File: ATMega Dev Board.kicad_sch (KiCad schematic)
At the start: 48 parts, among them J1 Conn_01x13, J2 Conn_01x09, J4 SPI header, J5 USB-C_31-M-12, Q1 S8050, Q2 2N7002, Q3 HL6042, Q4 HL6042, SW1 SW_SPST, SW2 SW_SPST, U1 ATmega32A-A, U2 CH340C, U3 USBLC6-2P6, X1 16MHz

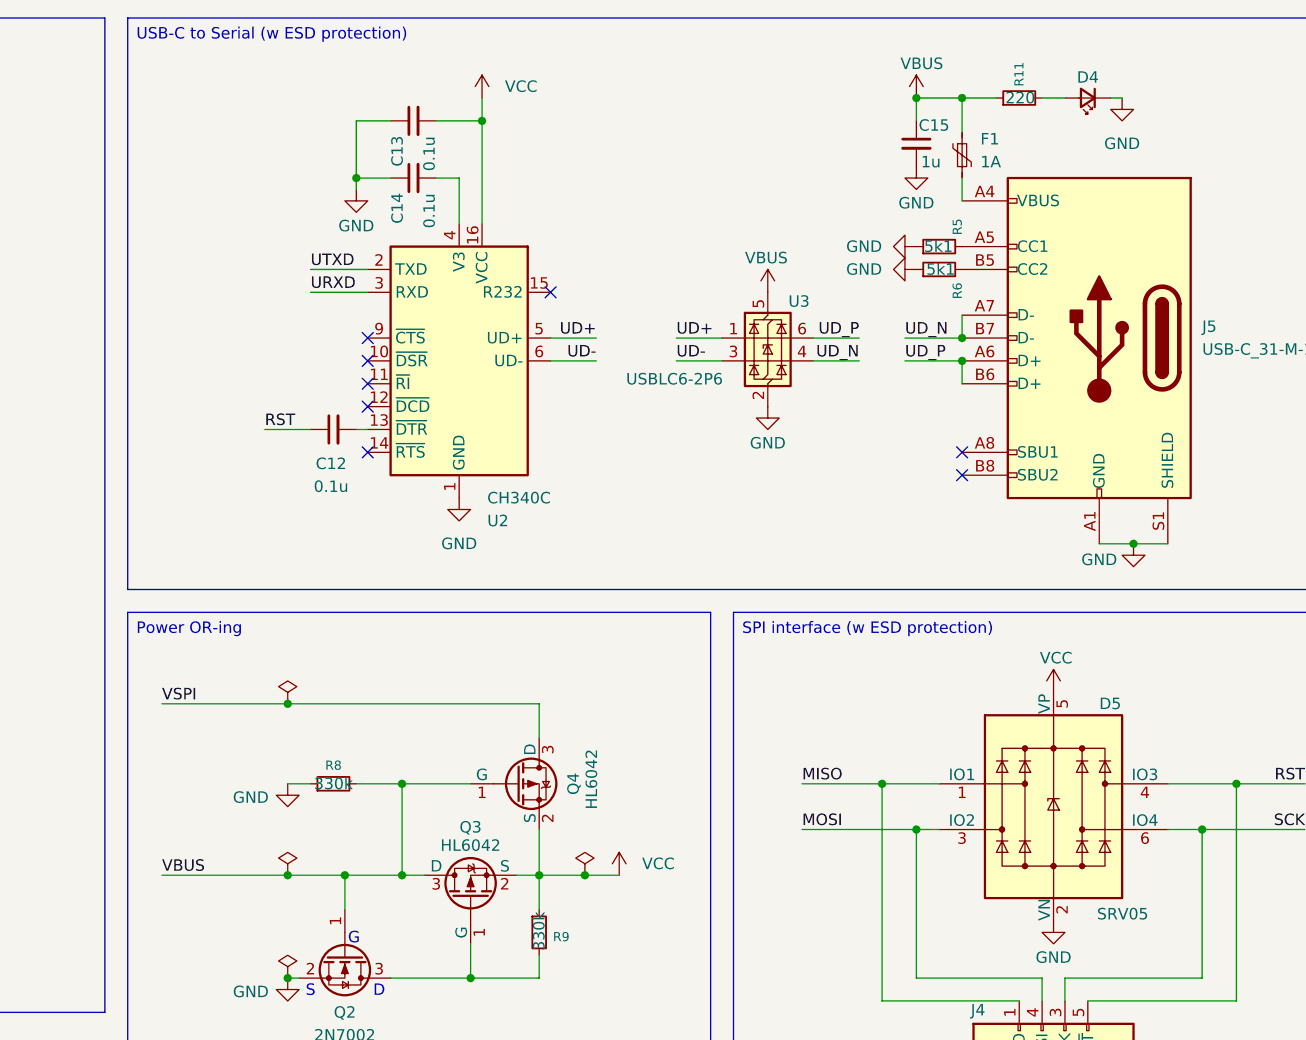
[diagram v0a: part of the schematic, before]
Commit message: better vbus power layout
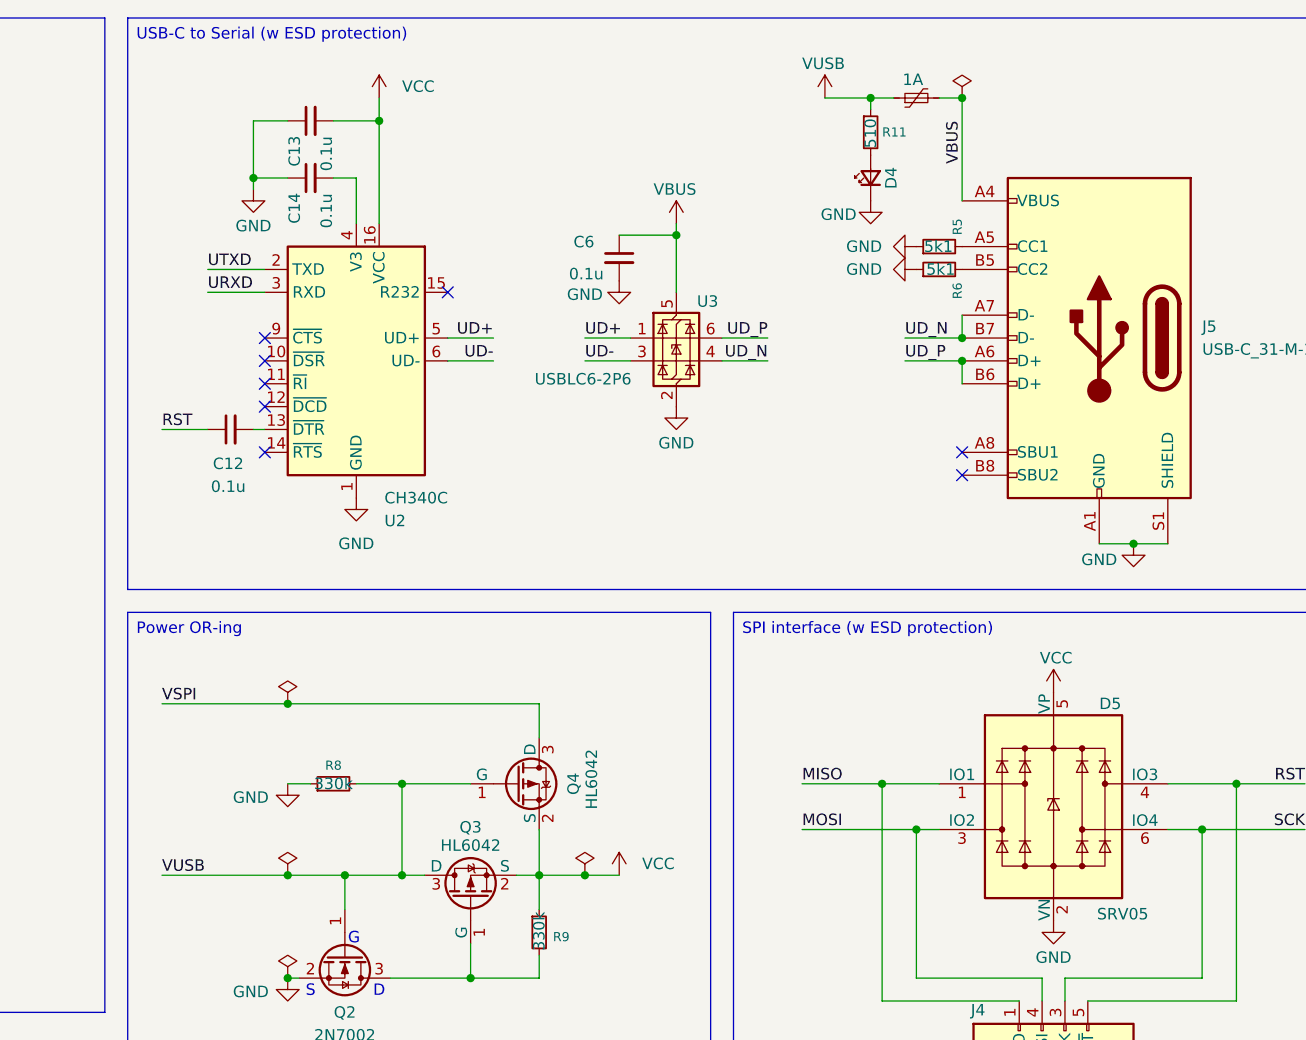
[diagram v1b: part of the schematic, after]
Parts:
- removed C15: 1u, Capacitor_SMD:C_0603_1608Metric, symbol Device:C_Small
- added C6: 0.1u, Capacitor_SMD:C_0603_1608Metric, symbol Device:C_Small
- J1, J2: now left out of the parts list
- Q3, Q4: footprint PCM_JLCPCB:Q_SOT-23 -> Package_TO_SOT_SMD:SOT-23
- R11: value 220 -> 510; LCSC C22962 -> C23193
- R5: footprint Resistor_SMD:R_0402_1005Metric -> Resistor_SMD:R_0603_1608Metric; LCSC C25905 -> C23186
- R6: footprint Resistor_SMD:R_0402_1005Metric -> Capacitor_SMD:C_0603_1608Metric; LCSC C25905 -> C23186
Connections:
- net GND: now also C6.2
- net VBUS: now also F1.2, J5.A4 (VBUS), J5.A9 (VBUS), J5.B4 (VBUS), J5.B9 (VBUS), C6.1; no longer F1.1, Q2.1 (G), Q3.3 (D), Q4.1 (G), R11.1, R8.2
- new net VUSB: F1.1, Q2.1 (G), Q3.3 (D), Q4.1 (G), R11.1, R8.2
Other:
- moved on the sheet: C12, C13, C14, D4, R11, U2, U3

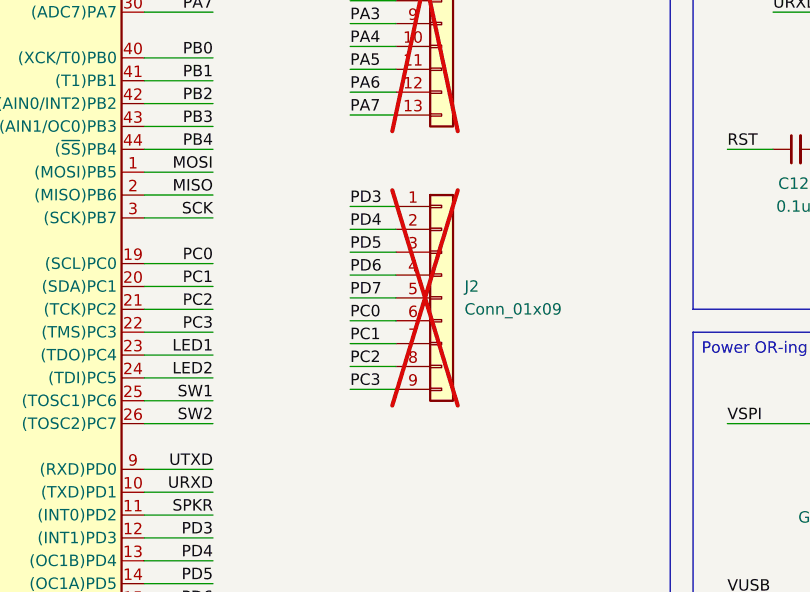
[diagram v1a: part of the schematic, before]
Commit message: exposed VCC and GND
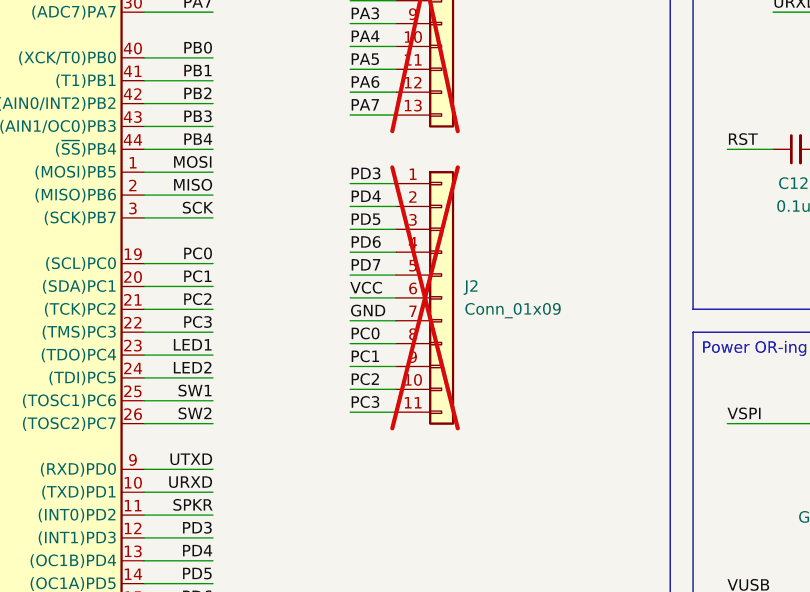
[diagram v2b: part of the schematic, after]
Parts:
- J2: footprint Connector_PinSocket_2.54mm:PinSocket_1x09_P2.54mm_Vertical -> Connector_PinSocket_2.54mm:PinSocket_1x11_P2.54mm_Vertical; symbol Connector_Generic:Conn_01x09 -> Connector_Generic:Conn_01x11; now in the parts list
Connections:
- net GND: now also J2.7 (Pin_7)
- net PC0: now also J2.8 (Pin_8); no longer J2.6 (Pin_6)
- net PC1: now also J2.9 (Pin_9); no longer J2.7 (Pin_7)
- net PC2: now also J2.10 (Pin_10); no longer J2.8 (Pin_8)
- net PC3: now also J2.11 (Pin_11); no longer J2.9 (Pin_9)
- net VCC: now also J2.6 (Pin_6)

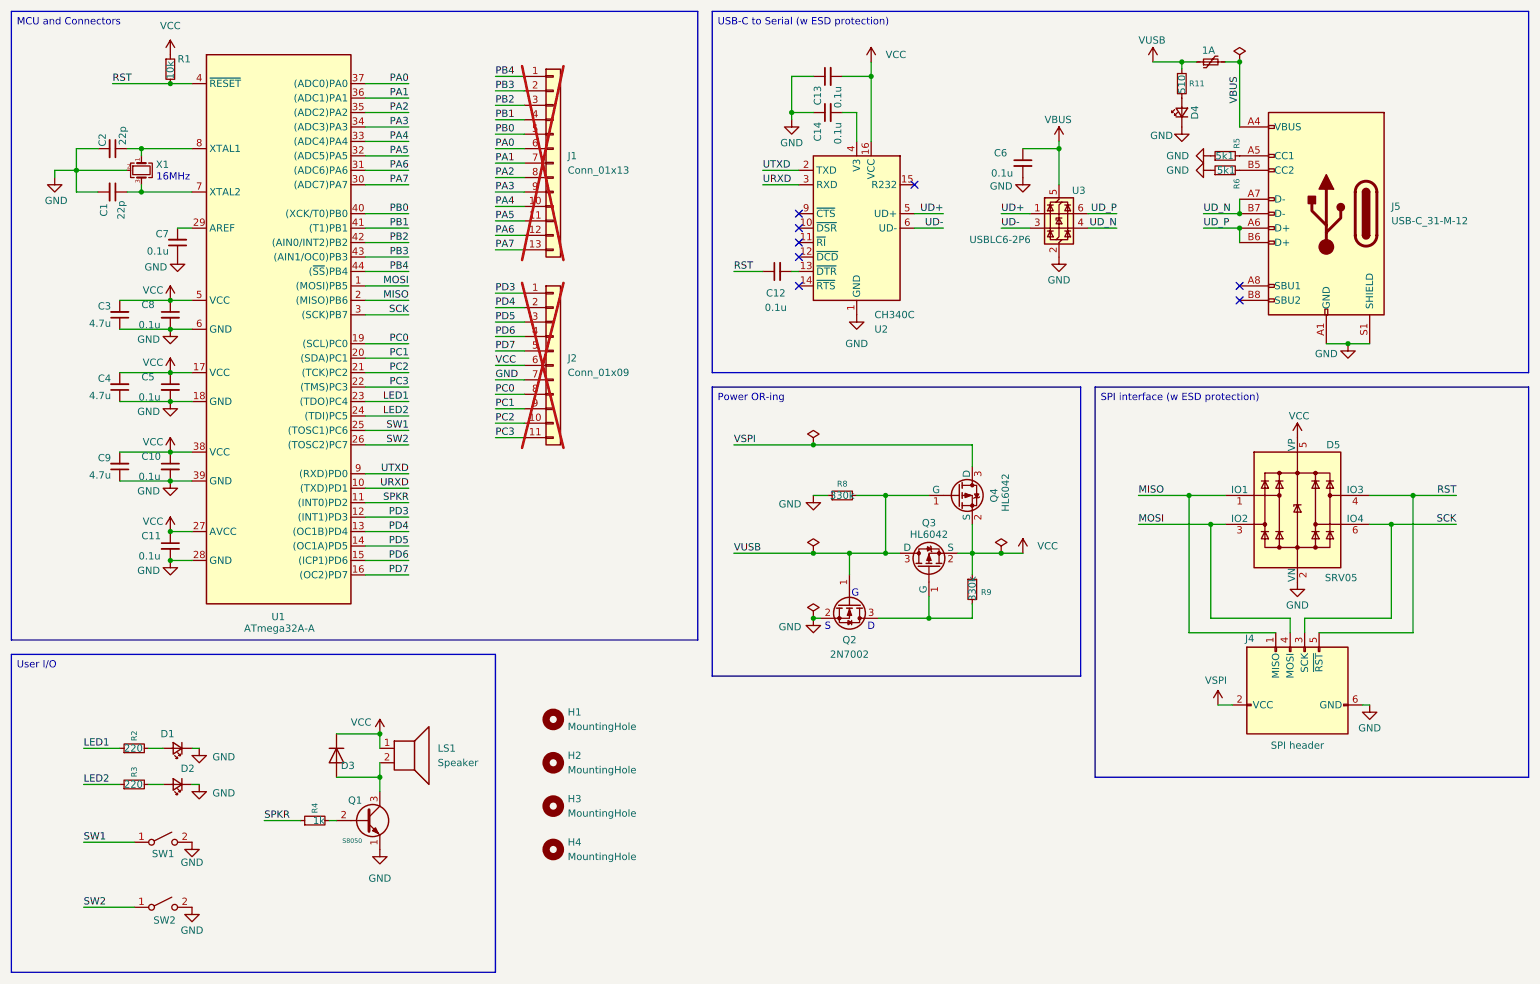
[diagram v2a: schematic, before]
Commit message: scl/sda pullups; better vcc filter
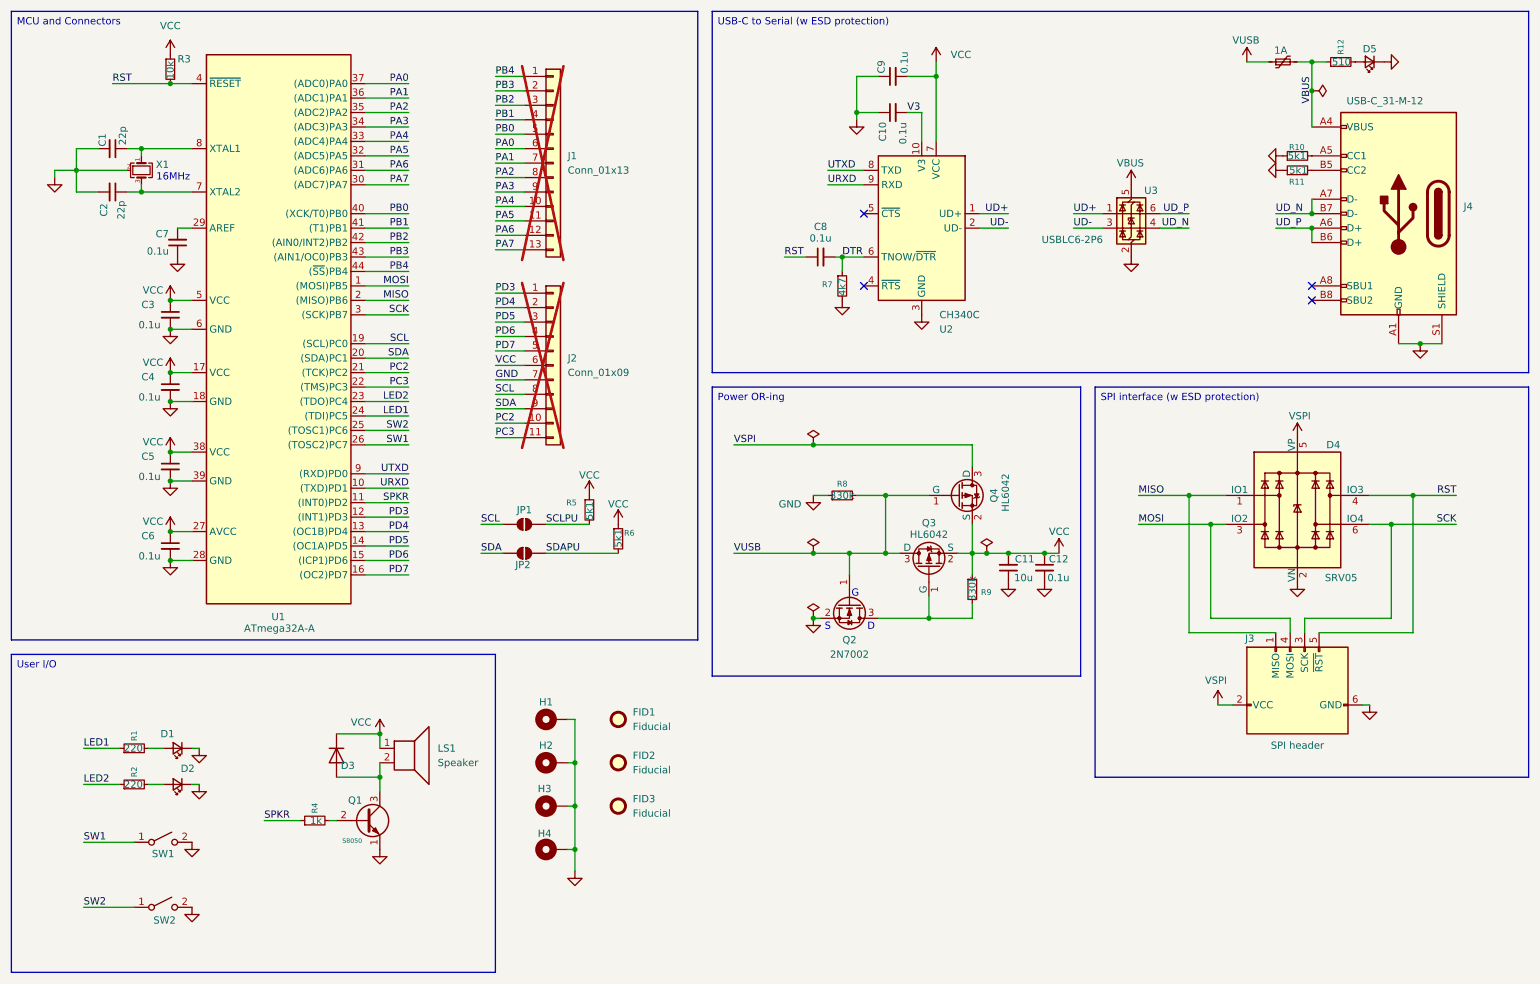
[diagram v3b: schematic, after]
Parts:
- removed C3, C4, C9: 4.7u, Capacitor_SMD:C_0603_1608Metric, symbol Device:C_Small
- removed C6: 0.1u, Capacitor_SMD:C_0603_1608Metric, symbol Device:C_Small
- added C11: 10u, Capacitor_SMD:C_0805_2012Metric, symbol Device:C_Small
- added C12: 0.1u, Capacitor_SMD:C_0603_1608Metric, symbol Device:C_Small
- added FID1, FID2, FID3: Fiducial, Fiducial:Fiducial_1mm_Mask2mm, symbol Mechanical:Fiducial
- added JP1, JP2: Jumper_2_Small_Open, Jumper:SolderJumper-2_P1.3mm_Open_Pad1.0x1.5mm, symbol Jumper:SolderJumper_2_Open
- added R5: 5k1, Capacitor_SMD:C_0603_1608Metric, symbol Device:R_Small
- added R6: 5k1, Resistor_SMD:R_0603_1608Metric, symbol Device:R_Small
- added R7: 4k7, Resistor_SMD:R_0603_1608Metric, symbol Device:R_Small
- H1, H2, H3, H4: footprint MountingHole:MountingHole_2.1mm -> MountingHole:MountingHole_3.2mm_M3_Pad_Via; symbol Mechanical:MountingHole -> Mechanical:MountingHole_Pad
- J4: renamed from J5; footprint FTBLib:USB_C_Receptacle_HRO_TYPE-C-31-M-12 -> ATMDBL:USB_C_Receptacle_HRO_TYPE-C-31-M-12
- LS1: footprint FTBLib:Buzzer_MLT-9650 -> ATMDBL:Buzzer_MLT-9650
- SW1, SW2: footprint FTBLib:Switch_TS-1088-AR02016 -> ATMDBL:Switch_TS-1088-AR02016
- U2: footprint Package_SO:SOIC-16_3.9x9.9mm_P1.27mm -> Package_SO:MSOP-10_3x3mm_P0.5mm; symbol Interface_USB:CH340C -> Interface_USB:CH340X
- renumbered C2 to C1, C14 to C10, C1 to C2, C8 to C3, C5 to C4, C10 to C5, C11 to C6, C12 to C8, C13 to C9, D5 to D4, D4 to D5, J4 to J3, R2 to R1, R5 to R10, R6 to R11, R11 to R12, R3 to R2, R1 to R3
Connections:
- net GND: now also H1.1, H2.1, H3.1, H4.1, U2.3 (GND), C11.1, C12.2, R7.2; no longer U2.1 (GND)
- net LED1: now also U1.24 ((TDI)PC5); no longer U1.23 ((TDO)PC4)
- net LED2: now also U1.23 ((TDO)PC4); no longer U1.24 ((TDI)PC5)
- net SW1: now also U1.26 ((TOSC2)PC7); no longer U1.25 ((TOSC1)PC6)
- net SW2: now also U1.25 ((TOSC1)PC6); no longer U1.26 ((TOSC2)PC7)
- net UD+: now also U2.1 (UD+); no longer U2.5 (UD+)
- net UD-: now also U2.2 (UD-); no longer U2.6 (UD-)
- net URXD: now also U2.9 (RXD); no longer U2.3 (RXD)
- net UTXD: now also U2.8 (TXD); no longer U2.2 (TXD)
- net VBUS: now also R12.1
- net VCC: now also U2.7 (VCC), C11.2, C12.1, R5.1, R6.1; no longer D4.5 (VP), U2.16 (VCC)
- net VSPI: now also D4.5 (VP)
- net VUSB: no longer R12.1
- net V3: now reaches U2.10 (V3)
- net V3: now also C10.2
- net DTR: now reaches C8.2
- net DTR: now also U2.6 (TNOW/~{DTR}), R7.1; no longer U2.13 (~{DTR})
- net at U2.4 (~{RTS}): no longer C10.2
- net PC0 renamed SCL
- net SCL: now also JP1.1 (A)
- net PC1 renamed SDA
- net SDA: now also JP2.1 (A)
- new net SCLPU: JP1.2 (B), R5.2
- new net SDAPU: JP2.2 (B), R6.2
- no-connect marks 8 -> 4
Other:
- moved on the sheet: C10, C8, C9, D5, J4, R10, R11, R12, U3

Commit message: tweaked layout
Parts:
- added R13: 0R, Resistor_SMD:R_0603_1608Metric, symbol Device:R_Small
- C11: LCSC C19666 -> C15850
- Q3, Q4: symbol PCM_JLCPCB-Transistors:PMOS,HL6042 -> Device:Q_PMOS
- R11: footprint Capacitor_SMD:C_0603_1608Metric -> Resistor_SMD:R_0603_1608Metric; LCSC C23186 -> C21189
- R7: LCSC C23193 -> C23162
- U1: symbol FTBLib:ATmega32A-A -> ATMDBL:ATmega32A-A
- U2: value CH340C -> CH340X
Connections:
- net VCC: now also R13.2; no longer C11.2, Q3.2 (S), Q4.2 (S), R9.1
- net VSPI: now also Q4.D; no longer Q4.3 (D)
- net VUSB: now also Q3.D, Q4.G; no longer Q3.3 (D), Q4.1 (G)
- net at Q2.3 (D), R9.2: now also Q3.G; no longer Q3.1 (G)
- new net: C11.2, Q3.S, Q4.S, R13.1, R9.1
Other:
- moved on the sheet: C11, C12, Q2, R5, R8, R9
